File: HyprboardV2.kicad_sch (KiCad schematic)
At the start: 0 parts

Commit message: Crystal Oscilator, Flash Memory done! Started working on the breakout for GPIO pins
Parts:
- added C1, C11, C12, C2, C3, C4, C5, C6, C7, C8, C9: 0.1uF, symbol Device:C
- added C10: 1uF, symbol Device:C
- added C13, C14: 10uF, symbol Device:C
- added C15, C16: 15pF, symbol Device:C
- added J1: USB_C_Receptacle_USB2.0_14P, symbol Connector:USB_C_Receptacle_USB2.0_14P
- added R1, R2: 5.1K, symbol Device:R
- added R3, R4: 27, symbol Device:R
- added R5, R7: 1K, symbol Device:R
- added R6: 10K, symbol Device:R
- added SW1: SW_Push, symbol Switch:SW_Push
- added U1: RP2040, Package_DFN_QFN:QFN-56-1EP_7x7mm_P0.4mm_EP3.2x3.2mm, symbol MCU_RaspberryPi:RP2040
- added U2: NCP1117-3.3_SOT223, Package_TO_SOT_SMD:SOT-223-3_TabPin2, symbol Regulator_Linear:NCP1117-3.3_SOT223
- added U3: W25Q128JVS, Package_SO:SOIC-8_5.3x5.3mm_P1.27mm, symbol Memory_Flash:W25Q128JVS
- added Y1: 12 MHz, symbol Device:Crystal_GND24
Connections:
- new net: J1.A5 (CC1), R1.1
- new net: R3.1, U1.46 (USB_DM)
- new net: R4.1, U1.47 (USB_DP)
- new net: R7.1, SW1.2
- new net: C16.2, R5.1, Y1.1
- new net: C13.2, C14.2
- new net: J1.B5 (CC2), R2.1
- new net +1V1: C10.1, C11.1, C12.1, U1.43 (ADC_AVDD), U1.48 (USB_VDD)
- new net +3V3: C1.1, C14.1, C2.1, C3.1, C4.1, C5.1, C6.1, C7.1, C8.1, C9.1, R6.1, U1.1 (IOVDD), U1.10 (IOVDD), U1.22 (IOVDD), U1.23 (DVDD), U1.33 (IOVDD), U1.42 (IOVDD), U1.44 (VREG_VIN), U1.45 (VREG_VOUT), U1.49 (IOVDD), U1.50 (DVDD), U2.2 (VO), U3.8 (VCC)
- new net GND: C1.2, C10.2, C11.2, C12.2, C15.1, C16.1, C2.2, C3.2, C4.2, C5.2, C6.2, C7.2, C8.2, C9.2, J1.A1 (GND), J1.A12 (GND), J1.B1 (GND), J1.B12 (GND), J1.S1 (SHIELD), R1.2, R2.2, SW1.1, U2.1 (GND), U3.4 (GND), Y1.2 (G), Y1.4 (G)
- new net QSPI_SCLK: U1.52 (QSPI_SCLK), U3.6 (CLK)
- new net QSPI_SD0: U1.53 (QSPI_SD0), U3.5 (DI/IO_{0})
- new net QSPI_SD1: U1.55 (QSPI_SD1), U3.2 (DO/IO_{1})
- new net QSPI_SD2: U1.54 (QSPI_SD2), U3.3 (~{WP}/IO_{2})
- new net QSPI_SD3: U1.51 (QSPI_SD3), U3.7 (~{HOLD}/~{RESET}/IO_{3})
- new net QSPI_SS: R6.2, R7.2, U1.56 (~{QSPI_SS}), U3.1 (~{CS})
- new net USD_D+: J1.A6 (D+), J1.B6 (D+), R3.2
- new net USD_D-: J1.A7 (D-), J1.B7 (D-), R4.2
- new net VBUS: C13.1, J1.A4 (VBUS), J1.A9 (VBUS), J1.B4 (VBUS), J1.B9 (VBUS), U2.3 (VI)
- new net XIN: C15.2, U1.20 (XIN), Y1.3
- new net XOUT: R5.2, U1.21 (XOUT)
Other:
- note added: "CRYSTAL OSCILLATOR"
- note added: "USB"

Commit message: Finished up the schematic
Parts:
- added C17: 0.1uF, Capacitor_SMD:C_0603_1608Metric, symbol Device:C
- added J2, J3: Conn_01x20, Connector_PinHeader_2.54mm:PinHeader_1x20_P2.54mm_Vertical, symbol Connector_Generic:Conn_01x20
- added J4: Conn_01x03, Connector_PinHeader_2.54mm:PinHeader_1x03_P2.54mm_Vertical, symbol Connector_Generic:Conn_01x03
- C1, C10, C11, C12, C2, C3, C4, C5, C6, C7, C8, C9: footprint (none) -> Capacitor_SMD:C_0402_1005Metric
- C13, C14: footprint (none) -> Capacitor_SMD:C_0603_1608Metric
- C15, C16: value 15pF -> 33pF; footprint (none) -> Capacitor_SMD:C_0603_1608Metric
- J1: footprint (none) -> Connector_USB:USB_C_Receptacle_HRO_TYPE-C-31-M-12
- R1, R2, R3, R4, R5, R6, R7: footprint (none) -> Resistor_SMD:R_0402_1005Metric
- SW1: footprint (none) -> Connector_PinHeader_2.54mm:PinHeader_1x20_P2.54mm_Vertical
- Y1: footprint (none) -> Crystal:Crystal_SMD_3225-4Pin_3.2x2.5mm
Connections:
- net +1V1: now also U1.23 (DVDD), U1.45 (VREG_VOUT), U1.50 (DVDD); no longer U1.43 (ADC_AVDD), U1.48 (USB_VDD)
- net +3V3: now also U1.43 (ADC_AVDD), U1.48 (USB_VDD), C17.1, J3.5 (Pin_5); no longer U1.23 (DVDD), U1.45 (VREG_VOUT), U1.50 (DVDD)
- net GND: now also U1.19 (TESTEN), U1.57 (GND), C17.2, J2.13 (Pin_13), J2.18 (Pin_18), J2.3 (Pin_3), J2.8 (Pin_8), J3.13 (Pin_13), J3.18 (Pin_18), J3.3 (Pin_3), J3.8 (Pin_8), J4.2 (Pin_2)
- net VBUS: now also J3.1 (Pin_1)
- net GPIO8: now reaches U1.11 (GPIO8)
- net GPIO8: now also J2.11 (Pin_11)
- net GPIO9: now reaches U1.12 (GPIO9)
- net GPIO9: now also J2.12 (Pin_12)
- net GPIO10: now reaches U1.13 (GPIO10)
- net GPIO10: now also J2.14 (Pin_14)
- net GPIO11: now reaches U1.14 (GPIO11)
- net GPIO11: now also J2.15 (Pin_15)
- net GPIO12: now reaches U1.15 (GPIO12)
- net GPIO12: now also J2.16 (Pin_16)
- net GPIO13: now reaches U1.16 (GPIO13)
- net GPIO13: now also J2.17 (Pin_17)
- net GPIO14: now reaches U1.17 (GPIO14)
- net GPIO14: now also J2.19 (Pin_19)
- net GPIO15: now reaches U1.18 (GPIO15)
- net GPIO15: now also J2.20 (Pin_20)
- net GPIO0: now reaches U1.2 (GPIO0)
- net GPIO0: now also J2.1 (Pin_1)
- net SWCLK: now reaches U1.24 (SWCLK)
- net SWCLK: now also J4.1 (Pin_1)
- net SWD: now reaches U1.25 (SWDIO)
- net SWD: now also J4.3 (Pin_3)
- net RUN: now reaches U1.26 (RUN)
- net RUN: now also J3.11 (Pin_11)
- net GPIO16: now reaches U1.27 (GPIO16)
- net GPIO16: now also J3.20 (Pin_20)
- net GPIO17: now reaches U1.28 (GPIO17)
- net GPIO17: now also J3.19 (Pin_19)
- net GPIO18: now reaches U1.29 (GPIO18)
- net GPIO18: now also J3.17 (Pin_17)
- net GPIO1: now reaches U1.3 (GPIO1)
- net GPIO1: now also J2.2 (Pin_2)
- net GPIO19: now reaches U1.30 (GPIO19)
- net GPIO19: now also J3.16 (Pin_16)
- net GPIO20: now reaches U1.31 (GPIO20)
- net GPIO20: now also J3.15 (Pin_15)
- net GPIO21: now reaches U1.32 (GPIO21)
- net GPIO21: now also J3.14 (Pin_14)
- net GPIO22: now reaches U1.34 (GPIO22)
- net GPIO22: now also J3.12 (Pin_12)
- net GPIO23: now reaches U1.35 (GPIO23)
- net GPIO23: now also J3.10 (Pin_10)
- net GPIO24: now reaches U1.36 (GPIO24)
- net GPIO24: now also J3.9 (Pin_9)
- net GPIO26_ADC0: now reaches U1.38 (GPIO26/ADC0)
- net GPIO26_ADC0: now also J3.7 (Pin_7)
- net GPIO27_ADC1: now reaches U1.39 (GPIO27/ADC1)
- net GPIO27_ADC1: now also J3.6 (Pin_6)
- net GPIO2: now reaches U1.4 (GPIO2)
- net GPIO2: now also J2.4 (Pin_4)
- net GPIO28_ADC2: now reaches U1.40 (GPIO28/ADC2)
- net GPIO28_ADC2: now also J3.4 (Pin_4)
- net GPIO29_ADC3: now reaches U1.41 (GPIO29/ADC3)
- net GPIO29_ADC3: now also J3.2 (Pin_2)
- net GPIO3: now reaches U1.5 (GPIO3)
- net GPIO3: now also J2.5 (Pin_5)
- net GPIO4: now reaches U1.6 (GPIO4)
- net GPIO4: now also J2.6 (Pin_6)
- net GPIO5: now reaches U1.7 (GPIO5)
- net GPIO5: now also J2.7 (Pin_7)
- net GPIO6: now reaches U1.8 (GPIO6)
- net GPIO6: now also J2.9 (Pin_9)
- net GPIO7: now reaches U1.9 (GPIO7)
- net GPIO7: now also J2.10 (Pin_10)
- no-connect marks 0 -> 1
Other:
- note added: "BREAKOUT"
- note added: "DECOUPLING CAPACITORS"
- note added: "Flash storage"
- note added: "RP2040"
- note added: "USB-C"
- note removed: "USB"
- moved on the sheet: C1, C10, C11, C12, C13, C14, C15, C16, C2, C3, C4, C5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

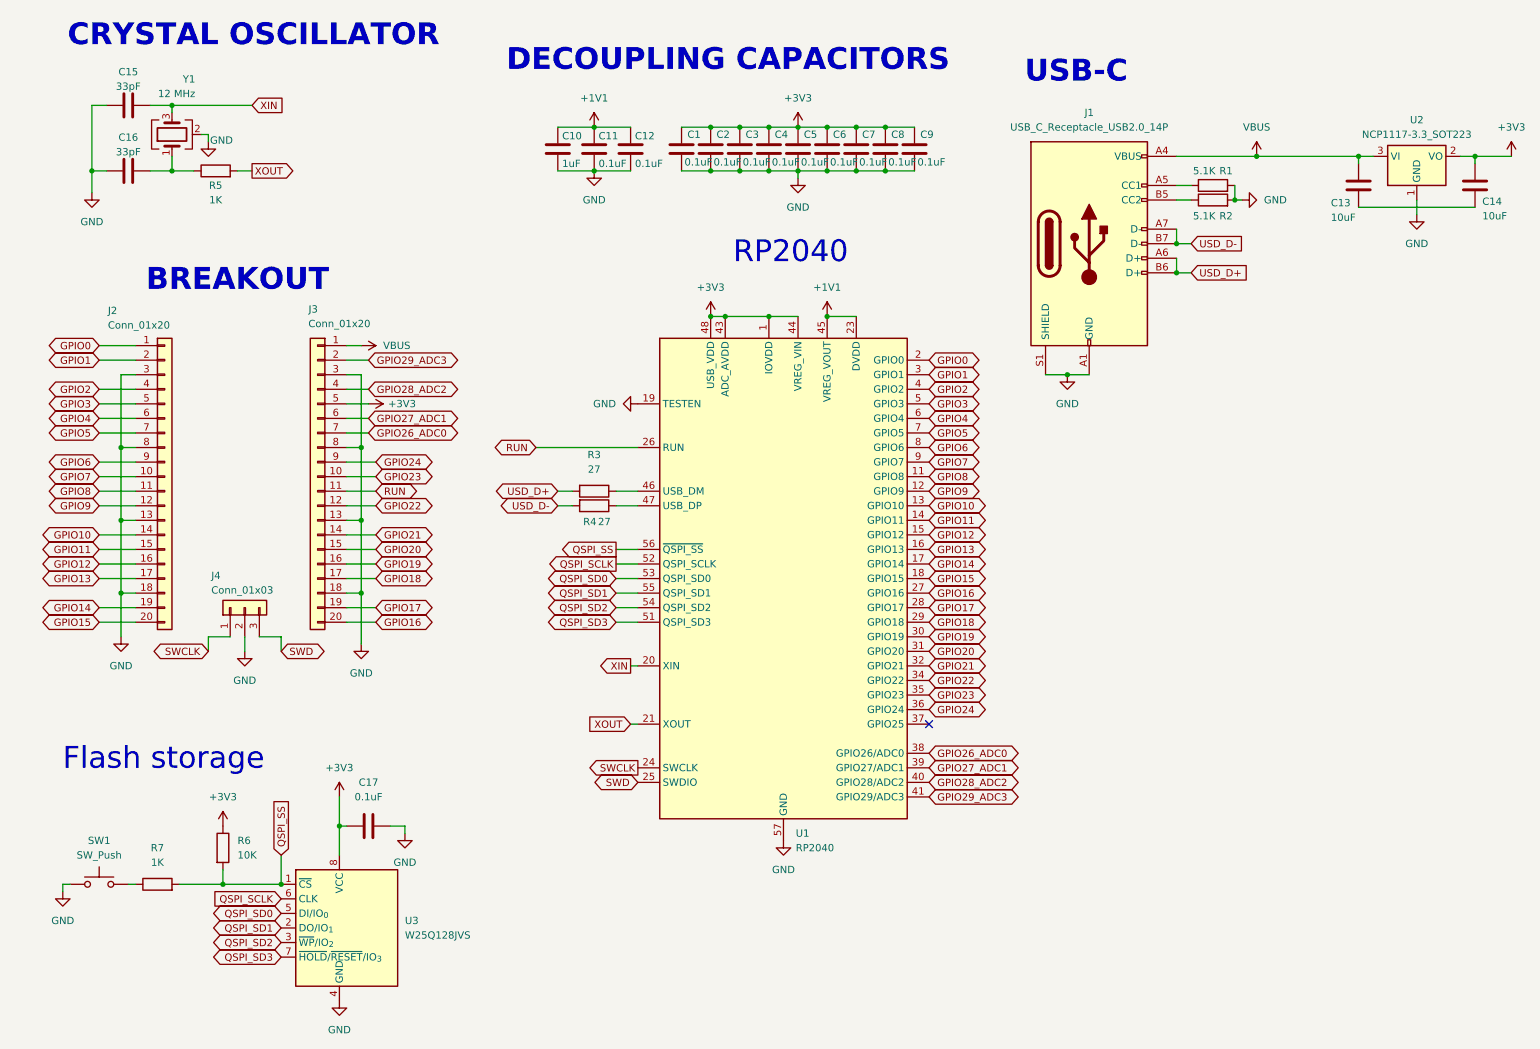
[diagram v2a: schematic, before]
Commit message: Changed the stuff Flash and USB components, 1/3rd positioned the components
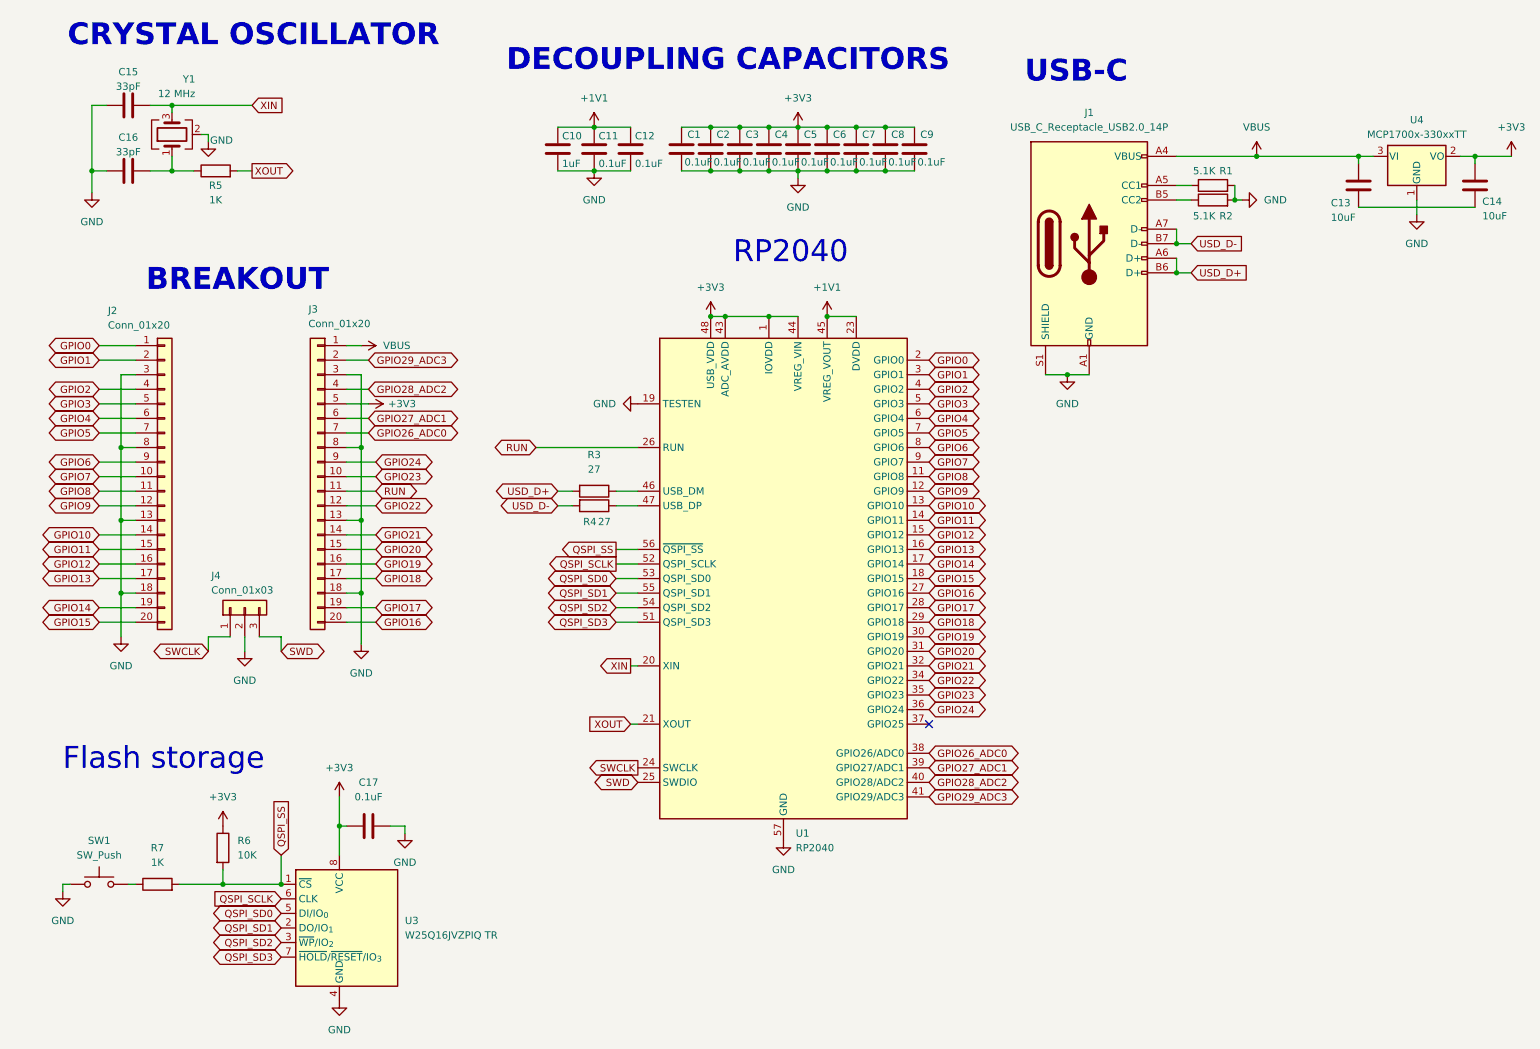
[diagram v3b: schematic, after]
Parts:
- removed U2: NCP1117-3.3_SOT223, Package_TO_SOT_SMD:SOT-223-3_TabPin2, symbol Regulator_Linear:NCP1117-3.3_SOT223
- added U4: MCP1700x-330xxTT, Package_TO_SOT_SMD:SOT-23, symbol Regulator_Linear:MCP1700x-330xxTT
- SW1: footprint Connector_PinHeader_2.54mm:PinHeader_1x20_P2.54mm_Vertical -> Button_Switch_SMD:SW_Push_SPST_NO_Alps_SKRK
- U3: value W25Q128JVS -> W25Q16JVZPIQ TR; footprint Package_SO:SOIC-8_5.3x5.3mm_P1.27mm -> Package_SON:Winbond_USON-8-1EP_3x2mm_P0.5mm_EP0.2x1.6mm
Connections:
- net +3V3: now also U4.2 (VO)
- net GND: now also U4.1 (GND)
- net VBUS: now also U4.3 (VI)
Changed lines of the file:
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@@
 			)
 		)
-		(property "Footprint" "Connector_PinHeader_2.54mm:PinHeader_1x20_P2.54mm_Vertical"
+		(property "Footprint" "Button_Switch_SMD:SW_Push_SPST_NO_Alps_SKRK"
 			(at 26.67 165.1 0)
 			(effects
@@
 	)
 	(symbol
-		(lib_id "Regulator_Linear:NCP1117-3.3_SOT223")
-		(at 256.54 43.18 0)
-		(unit 1)
-		(exclude_from_sim no)
-		(in_bom yes)
-		(on_board yes)
-		(dnp no)
-		(fields_autoplaced yes)
-		(property "Reference" "U2"
-			(at 256.54 36.83 0)
-			(effects
-				(font
-					(size 1.27 1.27)
-				)
-			)
-		)
-		(property "Value" "NCP1117-3.3_SOT223"
-			(at 256.54 39.37 0)
-			(effects
-				(font
-					(size 1.27 1.27)
-				)
-			)
-		)
-		(property "Footprint" "Package_TO_SOT_SMD:SOT-223-3_TabPin2"
-			(at 256.54 38.1 0)
-			(effects
-				(font
-					(size 1.27 1.27)
-				)
-				(hide yes)
-			)
-		)
-		(property "Datasheet" "http://www.onsemi.com/pub_link/Collateral/NCP1117-D.PDF"
-			(at 259.08 49.53 0)
-			(effects
-				(font
-					(size 1.27 1.27)
-				)
-				(hide yes)
-			)
-		)
-		(property "Description" "1A Low drop-out regulator, Fixed Output 3.3V, SOT-223"
-			(at 256.54 43.18 0)
-			(effects
-				(font
-					(size 1.27 1.27)
-				)
-				(hide yes)
-			)
-		)
-		(pin "2"
-		)
-		(pin "3"
-		)
-		(pin "1"
-		)
-		(instances
-			(project ""
-				(path "/262b1713-1fdd-4fc1-88ca-f4ad9a9f4d26"
-					(reference "U2")
-					(unit 1)
-				)
-			)
-		)
-	)
-	(symbol
 		(lib_id "power:GND")
 		(at 113.03 45.72 0)
@@
 			)
 		)
-		(property "Value" "W25Q128JVS"
+		(property "Value" "W25Q16JVZPIQ TR"
 			(at 80.01 179.0699 0)
 			(effects
@@
 			)
 		)
-		(property "Footprint" "Package_SO:SOIC-8_5.3x5.3mm_P1.27mm"
+		(property "Footprint" "Package_SON:Winbond_USON-8-1EP_3x2mm_P0.5mm_EP0.2x1.6mm"
 			(at 68.58 154.94 0)
 			(effects
@@
 					(unit 1)
 				)
+			)
+		)
+	)
+	(symbol
+		(lib_id "Regulator_Linear:MCP1700x-330xxTT")
+		(at 256.54 43.18 0)
+		(unit 1)
+		(exclude_from_sim no)
+		(in_bom yes)
+		(on_board yes)
+		(dnp no)
+		(fields_autoplaced yes)
+		(property "Reference" "U4"
+			(at 256.54 36.83 0)
+			(effects
+				(font
+					(size 1.27 1.27)
+				)
+			)
+		)
+		(property "Value" "MCP1700x-330xxTT"
+			(at 256.54 39.37 0)
+			(effects
+				(font
+					(size 1.27 1.27)
+				)
+			)
+		)
+		(property "Footprint" "Package_TO_SOT_SMD:SOT-23"
+			(at 256.54 37.465 0)
+			(effects
+				(font
+					(size 1.27 1.27)
+				)
+				(hide yes)
+			)
+		)
+		(property "Datasheet" "http://ww1.microchip.com/downloads/en/DeviceDoc/20001826D.pdf"
+			(at 256.54 43.18 0)
+			(effects
+				(font
+					(size 1.27 1.27)
+				)
+				(hide yes)
+			)
+		)
+		(property "Description" "250mA Low Quiscent Current LDO, 3.3V output, SOT-23"
+			(at 256.54 43.18 0)
+			(effects
+				(font
+					(size 1.27 1.27)
+				)
+				(hide yes)
+			)
+		)
+		(pin "1"
+		)
+		(pin "2"
+		)
+		(pin "3"
+		)
+		(instances
+			(project ""
+				(path "/262b1713-1fdd-4fc1-88ca-f4ad9a9f4d26"
+					(reference "U4")
+					(unit 1)
+				)

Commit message: DONE WITH THE ROUTINGGGgit add .! checkout stasis's journal for info
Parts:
- C17: footprint Capacitor_SMD:C_0603_1608Metric -> Capacitor_SMD:C_0402_1005Metric
- renumbered R2 to R1, R1 to R2, R7 to R6, R6 to R7, U4 to U2, U3 to U4
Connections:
- net GND: now also C13.2, C14.2
- net at U1.46 (USB_DM): now also R3.2; no longer R3.1
- net at U1.47 (USB_DP): now also R4.2; no longer R4.1
- net USD_D+ renamed USB_D+
- net USB_D+: now also R4.1; no longer R3.2
- net USD_D- renamed USB_D-
- net USB_D-: now also R3.1; no longer R4.2
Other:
- moved on the sheet: R3, R4
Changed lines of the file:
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@@
 	)
 	(junction
+		(at 256.54 52.07)
+		(diameter 0)
+		(color 0 0 0 0)
+	)
+	(junction
 		(at 148.59 45.72)
 		(diameter 0)
@@
 	(wire
 		(pts
-			(xy 246.38 52.07) (xy 266.7 52.07)
+			(xy 246.38 52.07) (xy 256.54 52.07)
 		)
 		(stroke
@@
 	(wire
 		(pts
-			(xy 256.54 53.34) (xy 256.54 50.8)
+			(xy 256.54 53.34) (xy 256.54 52.07)
 		)
 		(stroke
@@
 	(wire
 		(pts
+			(xy 256.54 52.07) (xy 266.7 52.07)
+		)
+		(stroke
+			(width 0)
+			(type default)
+		)
+	)
+	(wire
+		(pts
 			(xy 69.85 78.74) (xy 73.66 78.74)
 		)
@@
 	(wire
 		(pts
+			(xy 256.54 52.07) (xy 256.54 50.8)
+		)
+		(stroke
+			(width 0)
+			(type default)
+		)
+	)
+	(wire
+		(pts
 			(xy 26.67 116.84) (xy 33.02 116.84)
 		)
@@
 		)
 	)
-	(global_label "USD_D-"
+	(global_label "USB_D+"
 		(shape bidirectional)
 		(at 106.68 104.14 180)
@@
 		)
 	)
-	(global_label "USD_D+"
+	(global_label "USB_D-"
 		(shape bidirectional)
 		(at 106.68 101.6 180)
@@
 		)
 	)
-	(global_label "USD_D-"
-		(shape input)
+	(global_label "USB_D-"
+		(shape bidirectional)
 		(at 217.17 58.42 0)
 		(fields_autoplaced yes)
@@
 		)
 		(property "Intersheetrefs" "${INTERSHEET_REFS}"
-			(at 227.7752 58.42 0)
+			(at 228.8865 58.42 0)
 			(effects
 				(font
@@
 		)
 	)
-	(global_label "USD_D+"
-		(shape input)
+	(global_label "USB_D+"
+		(shape bidirectional)
 		(at 217.17 63.5 0)
 		(fields_autoplaced yes)
@@
 		)
 		(property "Intersheetrefs" "${INTERSHEET_REFS}"
-			(at 227.7752 63.5 0)
+			(at 228.8865 63.5 0)
 			(effects
 				(font
@@
 		(on_board yes)
 		(dnp no)
-		(property "Reference" "R1"
+		(property "Reference" "R2"
 			(at 223.266 45.72 90)
 			(effects
@@
 			(project ""
 				(path "/262b1713-1fdd-4fc1-88ca-f4ad9a9f4d26"
-					(reference "R1")
+					(reference "R2")
 					(unit 1)
 				)
@@
 	(symbol
 		(lib_id "Device:R")
-		(at 113.03 101.6 270)
+		(at 113.03 101.6 90)
 		(unit 1)
 		(exclude_from_sim no)
@@
 		(on_board yes)
 		(dnp no)
-		(fields_autoplaced yes)
 		(property "Reference" "R3"
-			(at 113.03 95.25 90)
+			(at 113.03 106.68 90)
 			(effects
 				(font
@@
 		)
 		(property "Value" "27"
-			(at 113.03 97.79 90)
+			(at 113.03 104.14 90)
 			(effects
 				(font
@@
 		)
 		(property "Footprint" "Resistor_SMD:R_0402_1005Metric"
-			(at 113.03 99.822 90)
+			(at 113.03 103.378 90)
 			(effects
 				(font
@@
 		(dnp no)
 		(fields_autoplaced yes)
-		(property "Reference" "R7"
+		(property "Reference" "R6"
 			(at 36.83 163.83 90)
 			(effects
@@
 			(project "HyprboardV2"
 				(path "/262b1713-1fdd-4fc1-88ca-f4ad9a9f4d26"
-					(reference "R7")
+					(reference "R6")
 					(unit 1)
 				)
@@
 			)
 		)
-		(property "Footprint" "Capacitor_SMD:C_0603_1608Metric"
+		(property "Footprint" "Capacitor_SMD:C_0402_1005Metric"
 			(at 77.47 159.0548 0)
 			(effects
@@
 	(symbol
 		(lib_id "Device:R")
-		(at 113.03 104.14 270)
+		(at 113.03 104.14 90)
 		(unit 1)
 		(exclude_from_sim no)
@@
 		(dnp no)
 		(property "Reference" "R4"
-			(at 112.268 106.934 90)
+			(at 113.792 101.346 90)
 			(effects
 				(font
@@
 		)
 		(property "Value" "27"
-			(at 114.808 106.934 90)
+			(at 111.252 101.346 90)
 			(effects
 				(font
@@
 		)
 		(property "Footprint" "Resistor_SMD:R_0402_1005Metric"
-			(at 113.03 102.362 90)
+			(at 113.03 105.918 90)
 			(effects
 				(font
@@
 		(dnp no)
 		(fields_autoplaced yes)
-		(property "Reference" "U3"
+		(property "Reference" "U4"
 			(at 80.01 176.5299 0)
 			(effects
@@
 			(project ""
 				(path "/262b1713-1fdd-4fc1-88ca-f4ad9a9f4d26"
-					(reference "U3")
+					(reference "U4")
 					(unit 1)
 				)
@@
 		(on_board yes)
 		(dnp no)
-		(property "Reference" "R2"
+		(property "Reference" "R1"
 			(at 223.266 53.594 90)
 			(effects
@@
 			(project "HyprboardV2"
 				(path "/262b1713-1fdd-4fc1-88ca-f4ad9a9f4d26"
-					(reference "R2")
+					(reference "R1")
 					(unit 1)
 				)
@@
 		(dnp no)
 		(fields_autoplaced yes)
-		(property "Reference" "R6"
+		(property "Reference" "R7"
 			(at 50.8 162.5599 0)
 			(effects
@@
 			(project ""
 				(path "/262b1713-1fdd-4fc1-88ca-f4ad9a9f4d26"
-					(reference "R6")
+					(reference "R7")
 					(unit 1)
 				)
@@
 		(dnp no)
 		(fields_autoplaced yes)
-		(property "Reference" "U4"
+		(property "Reference" "U2"
 			(at 256.54 36.83 0)
 			(effects
@@
 			(project ""
 				(path "/262b1713-1fdd-4fc1-88ca-f4ad9a9f4d26"
-					(reference "U4")
+					(reference "U2")
 					(unit 1)
 				)
